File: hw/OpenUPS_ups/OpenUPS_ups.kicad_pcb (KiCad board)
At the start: 4 copper layers, 90 x 62 mm, 281 parts, among them J1001 USB4105-GF-A, J101 Barrel Jack, J102 XT30PW-M, J103 XT30PW-M, J104 S2B-PH-K_1x02, J105 S2B-PH-K_1x02, J106 Screw Terminal, J107 Screw Terminal, J108 Screw Terminal, J109 JST XH, J110 JST XH, J501 Conn_01x03, J701 0022053031, J702 0022053031, J901 Qwiic, J902 Qwiic, Q301 AON7534, Q302 AON7534, Q303 AON7534, Q304 AON7534, Q401 2N7002, Q402 AON7534, Q403 AON7534, Q404 AON7534, Q405 AON7534, Q601 AON7534, Q602 AON7534, Q603 AON7534, Q604 AON7534, Q701 2N7002, Q702 2N7002, U1001 MCP6547, U1002 AP22814BW5, U101 AVR32DB48x-xPT, U201 TPS51397A, U202 INA180A3, U301 NCP81599, U401 NCP431, U402 BD99950, U403 MCP6001R, U404 DZDH0401DW, U405 INA180A1, U601 NCP81599, U801 AP7383-33W5, U901 π220N31

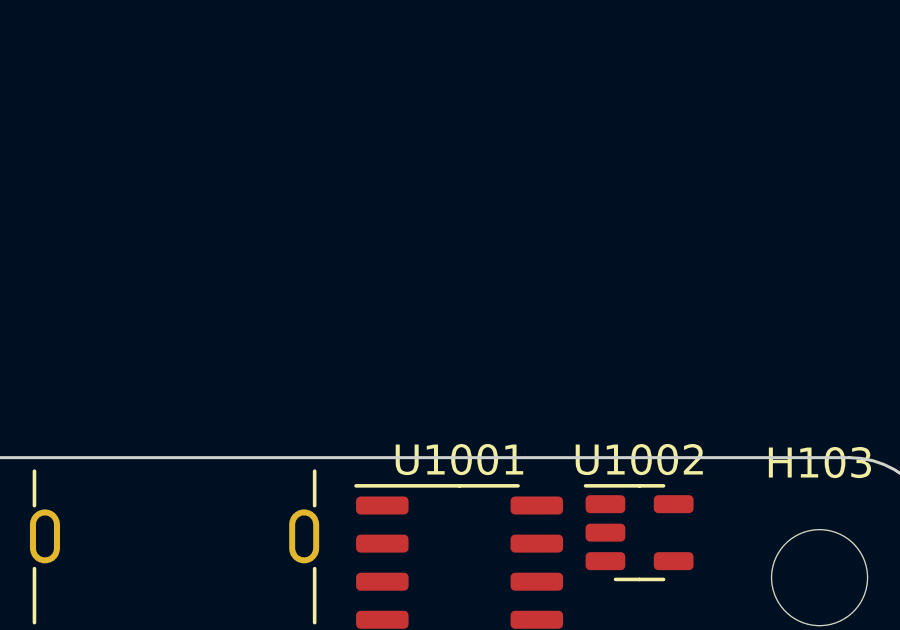
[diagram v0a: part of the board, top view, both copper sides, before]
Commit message: Issue #30: USB Force ON feature
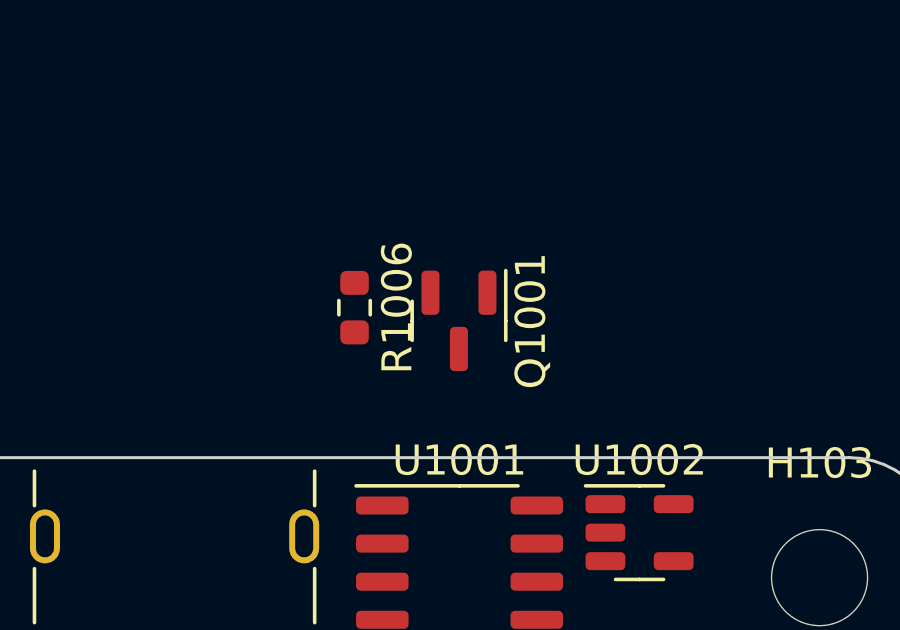
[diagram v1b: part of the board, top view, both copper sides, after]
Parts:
- added Q1001: 2N7002, Package_TO_SOT_SMD:SOT-23, F.Cu at (157.0, 67.4)
- added R1006: 10k, Resistor_SMD:R_0603_1608Metric, F.Cu at (153.5, 67.0)
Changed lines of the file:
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@@
   (net 69 "/Ext. I2C Interface/XI2C_GND")
   (net 70 "/Ext. I2C Interface/XI2C_VCC")
-  (net 71 "Net-(U1002-~{EN})")
+  (net 71 "Net-(Q1001-D)")
   (net 72 "Net-(U1001A--)")
   (net 73 "Net-(U301B-BST1)")
@@
   (net 202 "unconnected-(U1002-~{FLG}-Pad3)")
   (net 203 "Net-(R409-Pad1)")
+  (net 204 "/USB_FORCE")
   (footprint "Resistor_SMD:R_0603_1608Metric" (layer "F.Cu")
     (at 211.65 88.4)
@@
       (stroke (width 0.1) (type solid)) (layer "F.Fab"))
     (pad "1" smd roundrect (at -2.575 -1.905) (size 1.75 0.6) (layers "F.Cu" "F.Paste" "F.Mask") (roundrect_rratio 0.25)
-      (net 71 "Net-(U1002-~{EN})") (pintype "open_collector"))
+      (net 71 "Net-(Q1001-D)") (pintype "open_collector"))
     (pad "2" smd roundrect (at -2.575 -0.635) (size 1.75 0.6) (layers "F.Cu" "F.Paste" "F.Mask") (roundrect_rratio 0.25)
       (net 72 "Net-(U1001A--)") (pinfunction "-") (pintype "input"))
@@
       (net 72 "Net-(U1001A--)") (pinfunction "-") (pintype "input"))
     (pad "7" smd roundrect (at 2.575 -0.635) (size 1.75 0.6) (layers "F.Cu" "F.Paste" "F.Mask") (roundrect_rratio 0.25)
-      (net 71 "Net-(U1002-~{EN})") (pintype "open_collector"))
+      (net 71 "Net-(Q1001-D)") (pintype "open_collector"))
     (pad "8" smd roundrect (at 2.575 -1.905) (size 1.75 0.6) (layers "F.Cu" "F.Paste" "F.Mask") (roundrect_rratio 0.25)
       (net 97 "+5V") (pinfunction "V+") (pintype "power_in"))
@@
       (stroke (width 0.1) (type solid)) (layer "F.Fab"))
     (pad "1" smd roundrect (at -0.825 0 270) (size 0.8 0.95) (layers "F.Cu" "F.Paste" "F.Mask") (roundrect_rratio 0.25)
-      (net 71 "Net-(U1002-~{EN})") (pintype "passive"))
+      (net 71 "Net-(Q1001-D)") (pintype "passive"))
     (pad "2" smd roundrect (at 0.825 0 270) (size 0.8 0.95) (layers "F.Cu" "F.Paste" "F.Mask") (roundrect_rratio 0.25)
       (net 97 "+5V") (pintype "passive"))
@@
       (net 202 "unconnected-(U1002-~{FLG}-Pad3)") (pinfunction "~{FLG}") (pintype "open_collector"))
     (pad "4" smd roundrect (at 1.1375 0.95) (size 1.325 0.6) (layers "F.Cu" "F.Paste" "F.Mask") (roundrect_rratio 0.25)
-      (net 71 "Net-(U1002-~{EN})") (pinfunction "~{EN}") (pintype "input"))
+      (net 71 "Net-(Q1001-D)") (pinfunction "~{EN}") (pintype "input"))
     (pad "5" smd roundrect (at 1.1375 -0.95) (size 1.325 0.6) (layers "F.Cu" "F.Paste" "F.Mask") (roundrect_rratio 0.25)
       (net 97 "+5V") (pinfunction "IN") (pintype "power_in"))
@@
     )
   )
+  (footprint "Resistor_SMD:R_0603_1608Metric" (layer "F.Cu")
+    (at 153.5 67 -90)
+    (descr "Resistor SMD 0603 (1608 Metric), square (rectangular) end terminal, IPC_7351 nominal, (Body size source: IPC-SM-782 page 72, https://www.pcb-3d.com/wordpress/wp-content/uploads/ipc-sm-782a_amendment_1_and_2.pdf), generated with kicad-footprint-generator")
+    (tags "resistor")
+    (property "Sheetfile" "usbc.kicad_sch")
+    (property "Sheetname" "USB-C")
+    (property "ki_description" "Resistor, small symbol")
+    (property "ki_keywords" "R resistor")
+    (attr smd)
+    (fp_text reference "R1006" (at 0 -1.43 90) (layer "F.SilkS")
+        (effects (font (size 1 1) (thickness 0.15)))
+    )
+    (fp_text value "10k" (at 0 1.43 90) (layer "F.Fab")
+        (effects (font (size 1 1) (thickness 0.15)))
+    )
+    (fp_text user "${REFERENCE}" (at 0 0 90) (layer "F.Fab")
+        (effects (font (size 0.4 0.4) (thickness 0.06)))
+    )
+    (fp_line (start -0.237258 -0.5225) (end 0.237258 -0.5225)
+      (stroke (width 0.12) (type solid)) (layer "F.SilkS"))
+    (fp_line (start -0.237258 0.5225) (end 0.237258 0.5225)
+      (stroke (width 0.12) (type solid)) (layer "F.SilkS"))
+    (fp_line (start -1.48 -0.73) (end 1.48 -0.73)
+      (stroke (width 0.05) (type solid)) (layer "F.CrtYd"))
+    (fp_line (start -1.48 0.73) (end -1.48 -0.73)
+      (stroke (width 0.05) (type solid)) (layer "F.CrtYd"))
+    (fp_line (start 1.48 -0.73) (end 1.48 0.73)
+      (stroke (width 0.05) (type solid)) (layer "F.CrtYd"))
+    (fp_line (start 1.48 0.73) (end -1.48 0.73)
+      (stroke (width 0.05) (type solid)) (layer "F.CrtYd"))
+    (fp_line (start -0.8 -0.4125) (end 0.8 -0.4125)
+      (stroke (width 0.1) (type solid)) (layer "F.Fab"))
+    (fp_line (start -0.8 0.4125) (end -0.8 -0.4125)
+      (stroke (width 0.1) (type solid)) (layer "F.Fab"))
+    (fp_line (start 0.8 -0.4125) (end 0.8 0.4125)
+      (stroke (width 0.1) (type solid)) (layer "F.Fab"))
+    (fp_line (start 0.8 0.4125) (end -0.8 0.4125)
+      (stroke (width 0.1) (type solid)) (layer "F.Fab"))
+    (pad "1" smd roundrect (at -0.825 0 270) (size 0.8 0.95) (layers "F.Cu" "F.Paste" "F.Mask") (roundrect_rratio 0.25)
+      (net 2 "GND") (pintype "passive"))
+    (pad "2" smd roundrect (at 0.825 0 270) (size 0.8 0.95) (layers "F.Cu" "F.Paste" "F.Mask") (roundrect_rratio 0.25)
+      (net 204 "/USB_FORCE") (pintype "passive"))
+    (model "${KICAD6_3DMODEL_DIR}/Resistor_SMD.3dshapes/R_0603_1608Metric.wrl"
+      (offset (xyz 0 0 0))
+      (scale (xyz 1 1 1))
+      (rotate (xyz 0 0 0))
+    )
+  )
   (footprint "Resistor_SMD:R_1206_3216Metric" (layer "F.Cu")
     (at 103 109.5 -90)
@@
       (stroke (width 0.1) (type solid)) (layer "F.Fab"))
     (pad "1" smd roundrect (at -0.775 0 270) (size 0.9 0.95) (layers "F.Cu" "F.Paste" "F.Mask") (roundrect_rratio 0.25)
-      (net 71 "Net-(U1002-~{EN})") (pintype "passive"))
+      (net 71 "Net-(Q1001-D)") (pintype "passive"))
     (pad "2" smd roundrect (at 0.775 0 270) (size 0.9 0.95) (layers "F.Cu" "F.Paste" "F.Mask") (roundrect_rratio 0.25)
       (net 2 "GND") (pintype "passive"))
@@
       (offset (xyz 0 0 0))
       (scale (xyz 1 1 1))
+      (rotate (xyz 0 0 0))
+    )
+  )
+  (footprint "Package_TO_SOT_SMD:SOT-23" (layer "F.Cu")
+    (at 156.980001 67.44 -90)
+    (descr "SOT, 3 Pin (https://www.jedec.org/system/files/docs/to-236h.pdf variant AB), generated with kicad-footprint-generator ipc_gullwing_generator.py")
+    (tags "SOT TO_SOT_SMD")
+    (property "Sheetfile" "usbc.kicad_sch")
+    (property "Sheetname" "USB-C")
+    (property "ki_description" "0.115A Id, 60V Vds, N-Channel MOSFET, SOT-23")
+    (property "ki_keywords" "N-Channel Switching MOSFET")
+    (attr smd)
+    (fp_text reference "Q1001" (at 0 -2.4 90) (layer "F.SilkS")
+        (effects (font (size 1 1) (thickness 0.15)))
+    )
+    (fp_text value "2N7002" (at 0 2.4 90) (layer "F.Fab")
+        (effects (font (size 1 1) (thickness 0.15)))
+    )
+    (fp_text user "${REFERENCE}" (at 0 0 90) (layer "F.Fab")
+        (effects (font (size 0.32 0.32) (thickness 0.05)))
+    )
+    (fp_line (start 0 -1.56) (end -1.675 -1.56)
+      (stroke (width 0.12) (type solid)) (layer "F.SilkS"))
+    (fp_line (start 0 -1.56) (end 0.65 -1.56)
+      (stroke (width 0.12) (type solid)) (layer "F.SilkS"))
+    (fp_line (start 0 1.56) (end -0.65 1.56)
+      (stroke (width 0.12) (type solid)) (layer "F.SilkS"))
+    (fp_line (start 0 1.56) (end 0.65 1.56)
+      (stroke (width 0.12) (type solid)) (layer "F.SilkS"))
+    (fp_line (start -1.92 -1.7) (end -1.92 1.7)
+      (stroke (width 0.05) (type solid)) (layer "F.CrtYd"))
+    (fp_line (start -1.92 1.7) (end 1.92 1.7)
+      (stroke (width 0.05) (type solid)) (layer "F.CrtYd"))
+    (fp_line (start 1.92 -1.7) (end -1.92 -1.7)
+      (stroke (width 0.05) (type solid)) (layer "F.CrtYd"))
+    (fp_line (start 1.92 1.7) (end 1.92 -1.7)
+      (stroke (width 0.05) (type solid)) (layer "F.CrtYd"))
+    (fp_line (start -0.65 -1.125) (end -0.325 -1.45)
+      (stroke (width 0.1) (type solid)) (layer "F.Fab"))
+    (fp_line (start -0.65 1.45) (end -0.65 -1.125)
+      (stroke (width 0.1) (type solid)) (layer "F.Fab"))
+    (fp_line (start -0.325 -1.45) (end 0.65 -1.45)
+      (stroke (width 0.1) (type solid)) (layer "F.Fab"))
+    (fp_line (start 0.65 -1.45) (end 0.65 1.45)
+      (stroke (width 0.1) (type solid)) (layer "F.Fab"))
+    (fp_line (start 0.65 1.45) (end -0.65 1.45)
+      (stroke (width 0.1) (type solid)) (layer "F.Fab"))
+    (pad "1" smd roundrect (at -0.9375 -0.95 270) (size 1.475 0.6) (layers "F.Cu" "F.Paste" "F.Mask") (roundrect_rratio 0.25)
+      (net 204 "/USB_FORCE") (pinfunction "G") (pintype "input"))
+    (pad "2" smd roundrect (at -0.9375 0.95 270) (size 1.475 0.6) (layers "F.Cu" "F.Paste" "F.Mask") (roundrect_rratio 0.25)
+      (net 2 "GND") (pinfunction "S") (pintype "passive"))
+    (pad "3" smd roundrect (at 0.9375 0 270) (size 1.475 0.6) (layers "F.Cu" "F.Paste" "F.Mask") (roundrect_rratio 0.25)
+      (net 71 "Net-(Q1001-D)") (pinfunction "D") (pintype "passive"))
+    (model "${KICAD6_3DMODEL_DIR}/Package_TO_SOT_SMD.3dshapes/SOT-23.wrl"
+      (offset (xyz 0 0 0))
+      (scale (xyz 1 1 1))

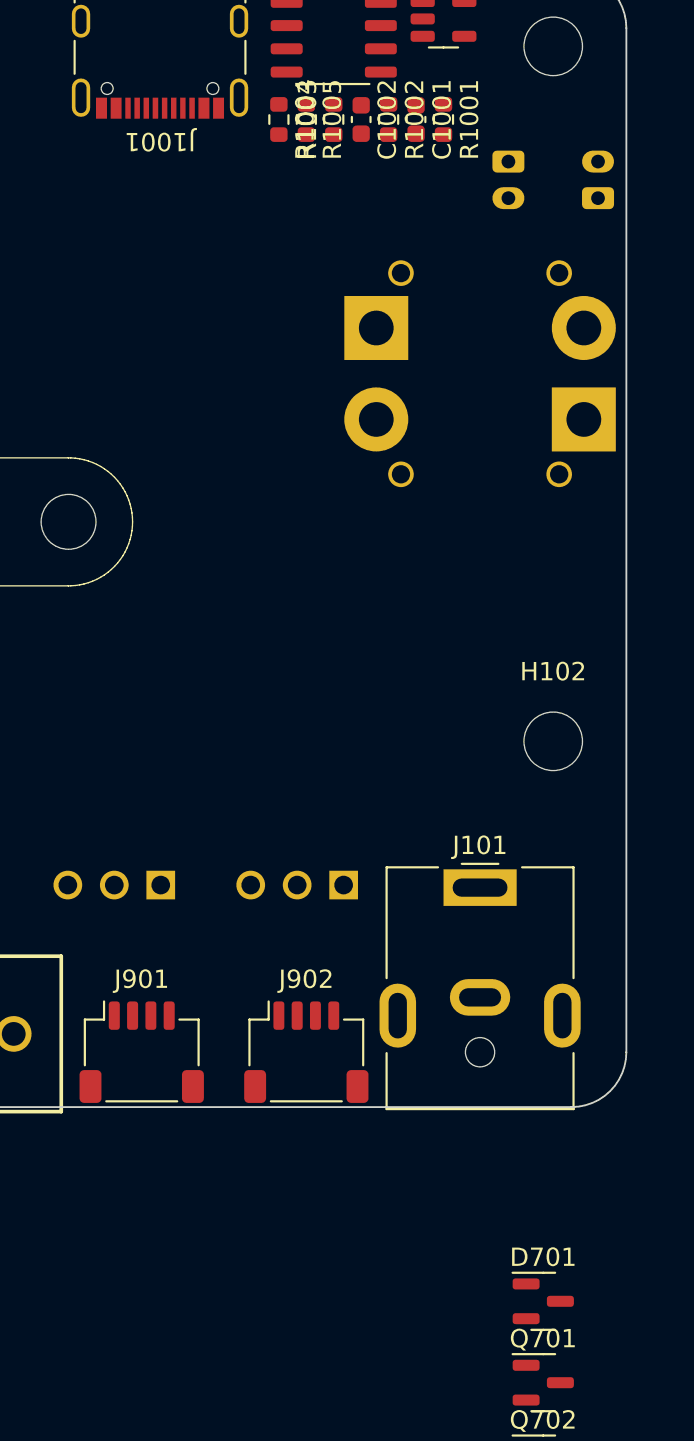
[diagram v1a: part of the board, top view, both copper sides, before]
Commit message: Issue #22 ESD protection on USB, Bat Data, Fans
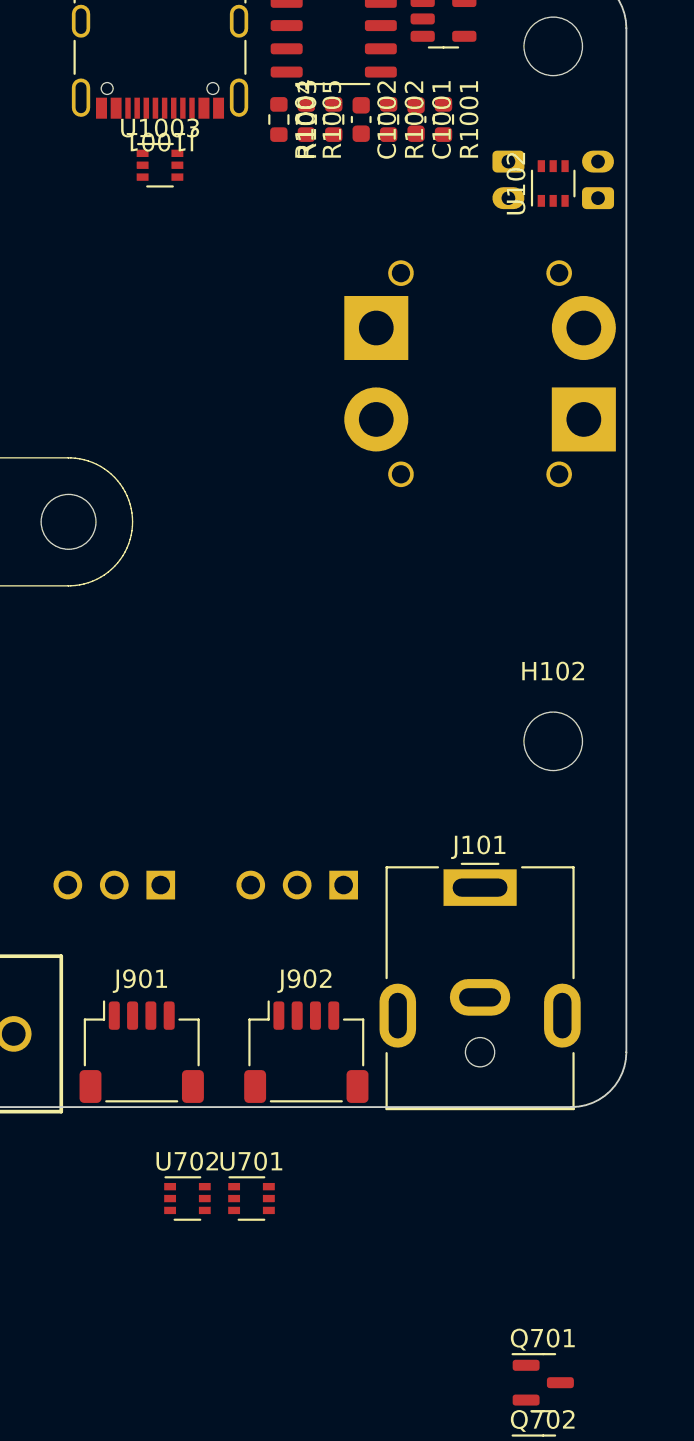
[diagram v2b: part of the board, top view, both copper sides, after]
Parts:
- removed D701: BAT54C, Package_TO_SOT_SMD:SOT-23
- added U1003: NUP2301MW6T1G, Package_TO_SOT_SMD:SOT-363_SC-70-6, F.Cu at (147.5, 82.5)
- added U102: NUP2301MW6T1G, Package_TO_SOT_SMD:SOT-363_SC-70-6, F.Cu at (169.0, 83.5)
- added U701: NUP2301MW6T1G, Package_TO_SOT_SMD:SOT-363_SC-70-6, F.Cu at (152.5, 139.0)
- added U702: NUP2301MW6T1G, Package_TO_SOT_SMD:SOT-363_SC-70-6, F.Cu at (149.0, 139.0)
